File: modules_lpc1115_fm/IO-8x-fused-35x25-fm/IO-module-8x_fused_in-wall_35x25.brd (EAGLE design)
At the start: 35 x 25 mm, 75 parts, among them IC1 LPC1115, IC2 ATAES132A-SHEQ-T, Q2 ASFL, U1 EEPROM, X3 MICROMATCH-10

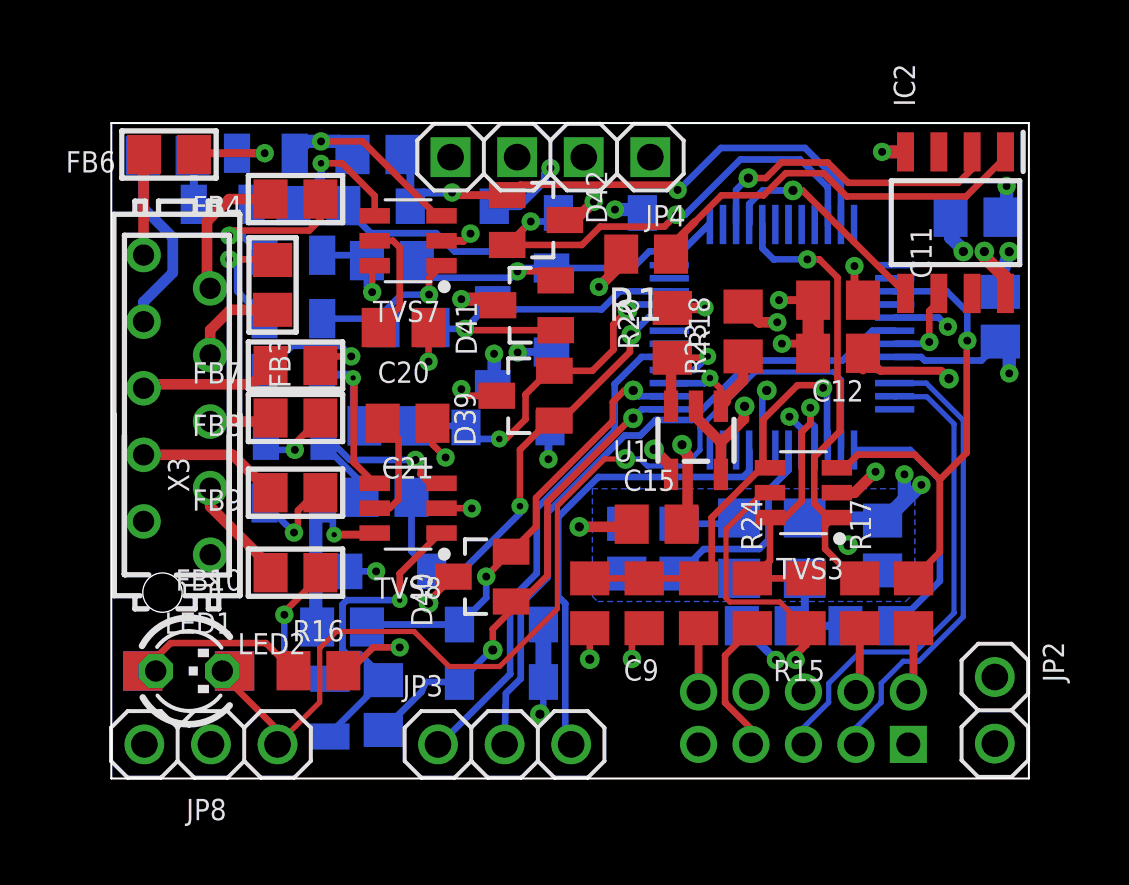
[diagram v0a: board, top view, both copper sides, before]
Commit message: [IOmodule8xUP]  moved power supply pins and SWD connector
consequences of changes in breakout board
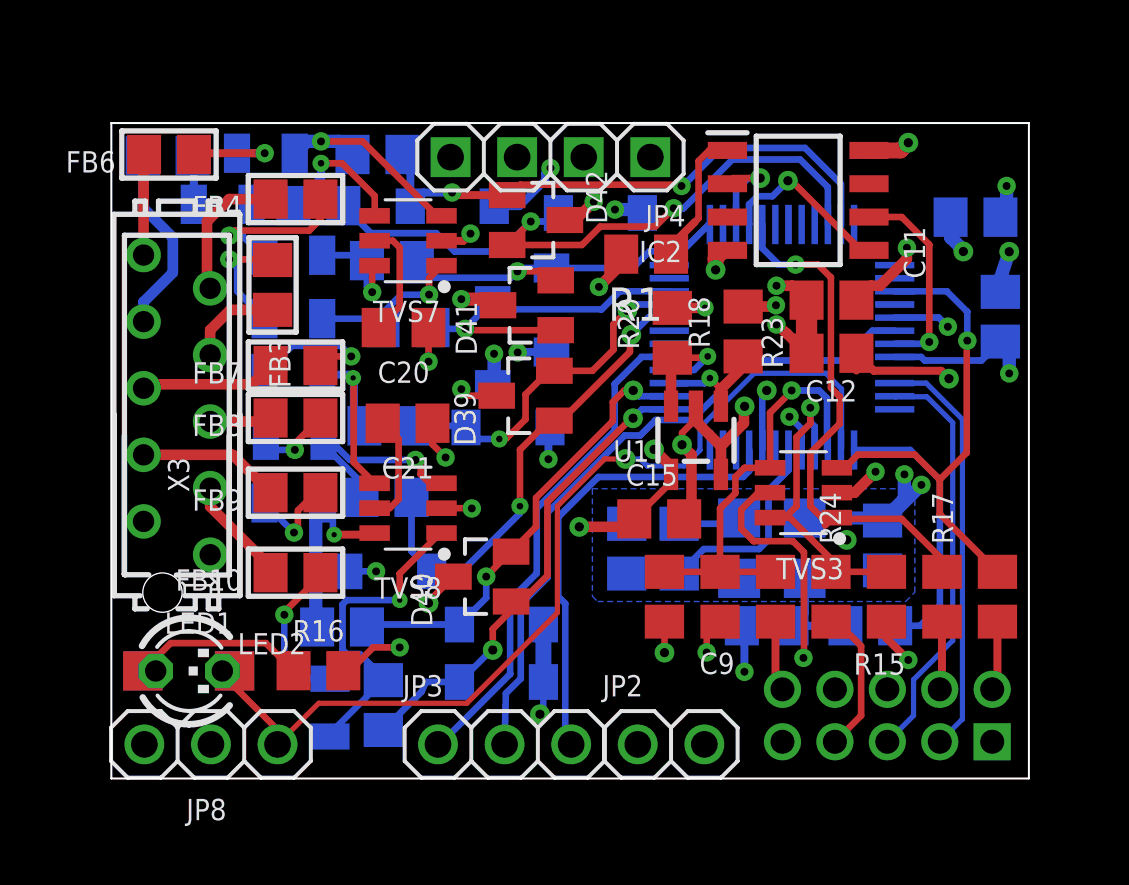
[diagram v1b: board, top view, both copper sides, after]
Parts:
- moved JP2 12.4 mm to (21.4, 1.30), turned to 0 degrees
- moved IC2 6.06 mm to (26.2, 22.1), turned to 0 degrees
- moved R19 3.21 mm to (33.8, 6.93)
- moved JP7 3.20 mm to (29.6, 2.40)
- moved R17 3.14 mm to (31.7, 6.93)
- moved R15 3.08 mm to (29.6, 6.93)
- moved R24 3.01 mm to (27.4, 6.93)
- moved R23 2.94 mm to (25.3, 6.93)
- moved C9 2.90 mm to (23.2, 6.93)
- moved R14 2.86 mm to (21.1, 6.93)
- moved C11 0.25 mm to (27.5, 18.2)
- moved C12 0.25 mm to (27.5, 16.2)
- moved C15 0.22 mm to (20.9, 9.90)
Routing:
- net N$19: track 15.4 -> 5.25 mm
- net MISO0: track 11.9 -> 3.75 mm
- net SCK1: track 3.35 -> 7.80 mm
- net GND: track 46.8 -> 50.6 mm
- net +3V3: track 53.3 -> 56.4 mm, vias 21 -> 22
- net SWCLK: track 17.6 -> 20.5 mm
- net ISP_TXD: track 18.5 -> 15.8 mm
- net PROG: track 39.9 -> 37.5 mm
- net ISP_RXD: track 17.6 -> 15.8 mm
- net MOSI0: track 8.59 -> 6.82 mm
- net ISP_EN: track 11.5 -> 13.1 mm
- net XTAL_EN: track 10.0 -> 10.6 mm

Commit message: [IOmodule8xUP]  added holes / change BB-fixing-pins from 4 to 2
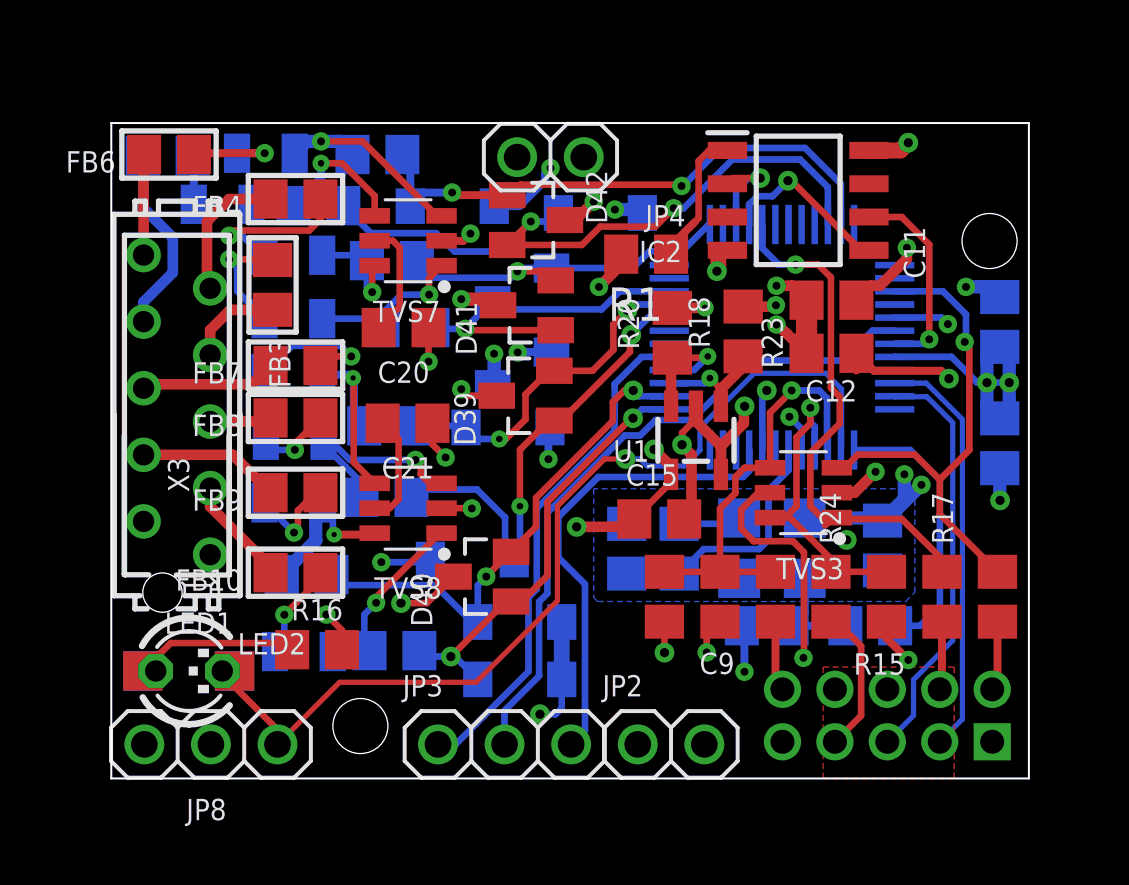
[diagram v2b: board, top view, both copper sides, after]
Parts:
- JP4: device pinhead_dmx:1X04 -> pinhead_dmx:1X02
- moved C13 4.83 mm to (33.9, 12.8), turned to 90 degrees
- moved C1 4.10 mm to (33.9, 17.4), turned to 270 degrees
- moved D35 3.18 mm to (13.8, 8.35)
- moved R45 2.41 mm to (7.45, 7.78)
- moved F21 2.36 mm to (7.34, 4.84), turned to 180 degrees
- moved R44 2.12 mm to (10.8, 4.88), turned to 180 degrees
- moved R16 0.80 mm to (7.85, 4.91)
- moved D37 0.71 mm to (15.6, 3.78)
- moved D38 0.71 mm to (15.6, 5.97)
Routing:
- net N$14: track 12.3 -> 7.26 mm
- net +3V3: track 56.4 -> 60.5 mm
- net IO2: track 16.9 -> 20.1 mm
- net N$7: track 5.89 -> 3.73 mm
- net IO1: track 18.4 -> 16.6 mm
- net N$20: track 7.89 -> 6.40 mm
- net GND: track 50.6 -> 51.9 mm
- added copper zone on layer 1, net NOGND

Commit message: [IOmodule8xUP] added JST ZH connector for I2C; reordered
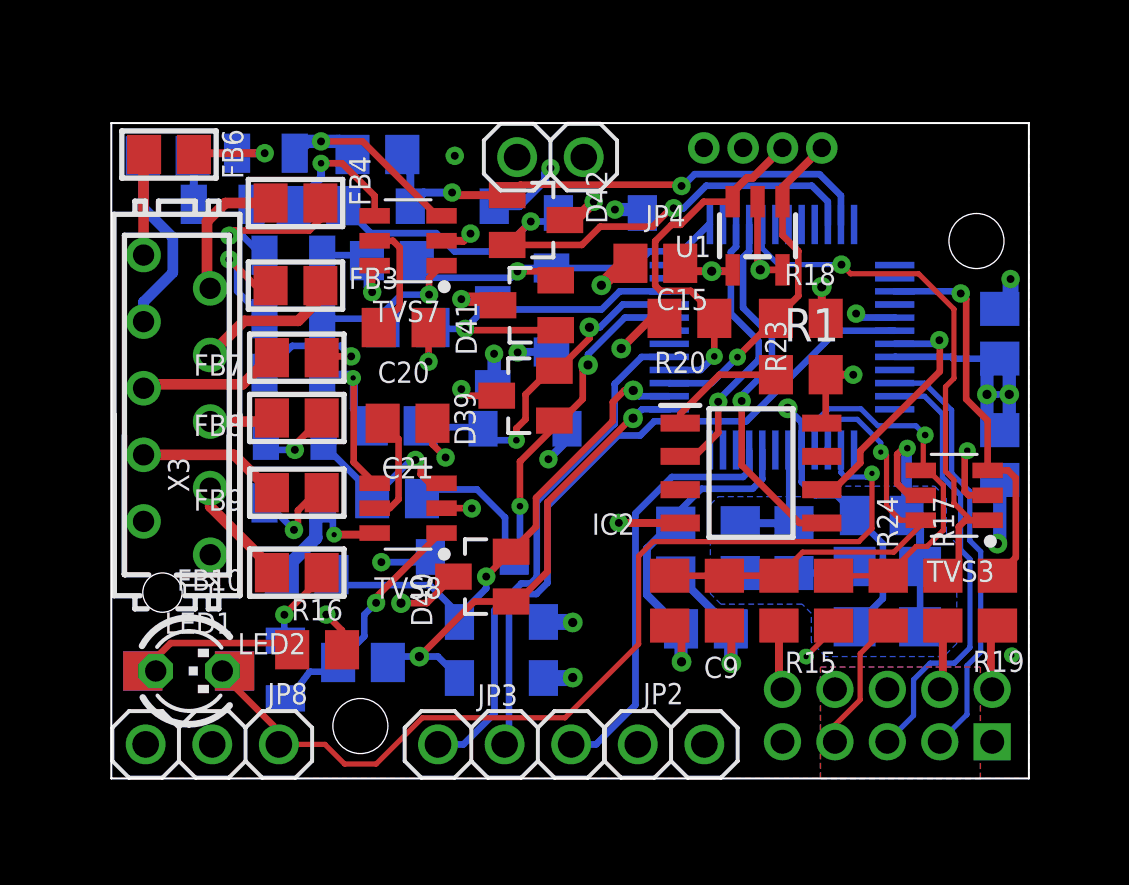
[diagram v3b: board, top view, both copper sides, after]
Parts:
- removed R26: 100k, rcl:R0805
- removed R27: 0R, rcl:R0805
- added JP1: B4B-ZR, jst:B4B-ZR
- moved C11 13.4 mm to (22.7, 5.71), flipped to the bottom, turned to 0 degrees
- moved IC2 10.6 mm to (24.4, 11.7)
- moved C15 9.75 mm to (20.8, 19.6), turned to 180 degrees
- moved C12 9.53 mm to (21.5, 8.77), flipped to the bottom, turned to 90 degrees
- moved U1 8.15 mm to (24.6, 20.7)
- moved R1 7.48 mm to (26.3, 15.4), turned to 0 degrees
- moved TVS3 5.75 mm to (32.1, 10.8)
- moved Q2 4.77 mm to (29.6, 6.94)
- moved C8 4.38 mm to (26.0, 8.79), turned to 270 degrees
- moved C7 4.33 mm to (24.0, 8.79), turned to 90 degrees
- moved R18 2.26 mm to (26.3, 17.6), turned to 0 degrees
- moved R24 2.19 mm to (29.6, 6.78)
- moved R15 2.02 mm to (27.5, 6.78)
- moved R44 1.28 mm to (9.60, 4.42)
- moved C14 1.15 mm to (29.4, 10.0), turned to 180 degrees
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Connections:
- removed net N$11: Q2.1, R26.1, R27.2
- net +3V3: now also JP1.2, Q2.1, X3.2; no longer R26.2, X3.1
- net GND: now also JP1.1, X3.1; no longer X3.2
- net ISP_EN: now also TVS3.4; no longer TVS3.6
- net RESET: now also TVS3.6; no longer TVS3.4
- net SCL: now also JP1.4
- net SDA: now also JP1.3
- net XTAL_EN: no longer R27.1
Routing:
- net XTAL_EN: track 10.6 -> 0.00 mm
- net SDA: track 4.93 -> 14.5 mm
- net SCL: track 5.13 -> 12.8 mm
- net +3V3: track 60.5 -> 52.9 mm, vias 22 -> 14
- net MOSI0: track 6.82 -> 14.2 mm
- net MISO0: track 3.75 -> 10.9 mm
- net XTALIN: track 9.68 -> 4.93 mm
- net SWDIO: track 19.0 -> 14.9 mm
- net N$11: track 4.07 -> 0.00 mm
- net GND: track 51.9 -> 54.5 mm
- net ISP_EN: track 13.1 -> 15.4 mm
- net N$14: track 7.26 -> 9.26 mm
- net IN5: track 3.65 -> 5.59 mm
- net IO1: track 16.6 -> 18.6 mm
- net EIB_IN: track 18.1 -> 16.2 mm
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- added copper zone on layer 1, net GND
- added copper zone on layer 16, net NOGND

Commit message: [IOmodule8xUP] massive re-arrangement
divided part so that 4 IOs are on TOP and 4 IOs on BOT
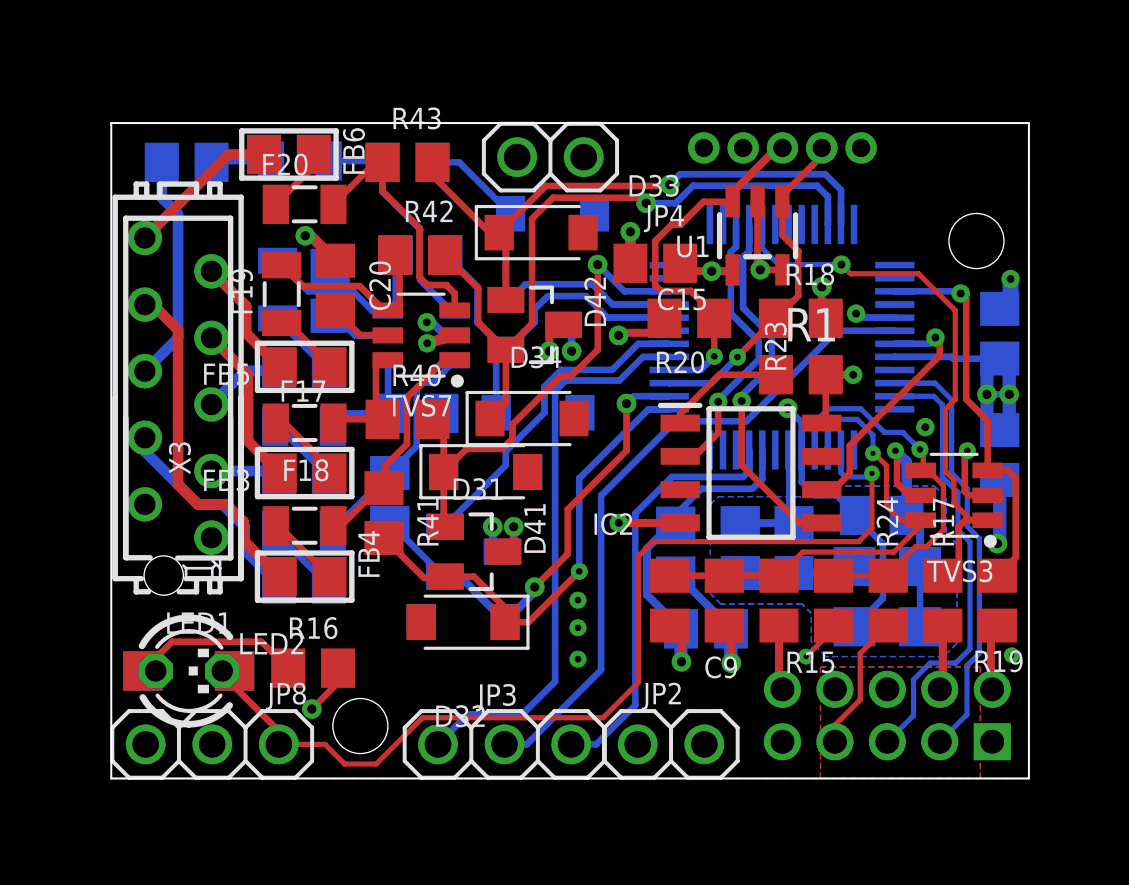
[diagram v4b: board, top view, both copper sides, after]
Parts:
- JP1: value B4B-ZR -> B5B-ZR; device jst:B4B-ZR -> jst:B5B-ZR
- moved FB4 14.3 mm to (7.38, 7.70)
- moved D32 12.4 mm to (13.4, 5.96), flipped to the top, turned to 180 degrees
- moved F18 10.3 mm to (7.38, 9.64), flipped to the top, turned to 0 degrees
- moved R47 10.1 mm to (11.3, 23.5)
- moved R44 9.72 mm to (11.7, 13.9)
- moved R41 9.63 mm to (10.4, 10.1), flipped to the top, turned to 270 degrees
- moved D41 9.61 mm to (13.8, 8.65), turned to 270 degrees
- moved FB5 9.60 mm to (7.38, 15.7), flipped to the top, turned to 180 degrees
- moved R46 9.34 mm to (11.8, 20.0)
- moved F21 9.31 mm to (7.35, 13.4), turned to 180 degrees
- moved FB7 8.55 mm to (2.88, 23.5), flipped to the bottom, turned to 0 degrees
- moved D36 8.27 mm to (16.8, 21.5)
- moved D34 8.26 mm to (16.0, 13.7), flipped to the top, turned to 0 degrees
- moved F24 8.10 mm to (7.20, 23.6)
- moved D37 7.87 mm to (14.3, 11.7)
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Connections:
- removed net IO114: IC1.10
- removed net N$14: F21.2, R44.1, TVS8.1
- removed net N$20: F22.2, R45.1, TVS8.6
- new net N$11: F18.2, R41.1, TVS7.1
- new net N$12: F17.2, R40.1, TVS7.6
- net IN6: now also X3.9; no longer X3.8
- net IN7: now also X3.8; no longer X3.9
- net IO1: now also D40.2, IC1.18; no longer D40.1, IC1.13
- net IO2: now also D40.1; no longer D40.2
- net IO6: now also IC1.13; no longer IC1.25
- net N$13: now also TVS8.6; no longer TVS8.3
- net N$16: now also F24.2, R47.1, TVS8.1; no longer F18.2, R41.1, TVS7.6
- net N$18: now also F21.2, R44.1, TVS8.4; no longer F17.2, R40.1, TVS7.1
- net N$9: now also F22.2, R45.1, TVS8.3; no longer F24.2, R47.1, TVS8.4
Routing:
- net GND: track 54.5 -> 40.8 mm, vias 23 -> 17
- net N$14: track 9.26 -> 0.00 mm, vias 1 -> 0
- net N$11: track 0.00 -> 8.77 mm
- net IN7: track 5.32 -> 13.3 mm
- net N$20: track 6.40 -> 0.00 mm, vias 1 -> 0
- net IO5: track 13.4 -> 18.8 mm
- net N$16: track 4.12 -> 8.97 mm, vias 1 -> 0
- net N$12: track 0.00 -> 4.60 mm
- net IO6: track 13.9 -> 18.0 mm
- net IO3: track 18.3 -> 14.9 mm, vias 2 -> 0
- net IN4: track 5.38 -> 8.75 mm
- net N$3: track 6.01 -> 2.85 mm, vias 1 -> 0
- net IN2: track 5.49 -> 8.26 mm
- net N$5: track 5.05 -> 2.29 mm, vias 1 -> 0
- net IN6: track 7.26 -> 4.73 mm
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
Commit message: [IOmodule8xUP]  optimized names & values positions; changed JP1 to 2mm
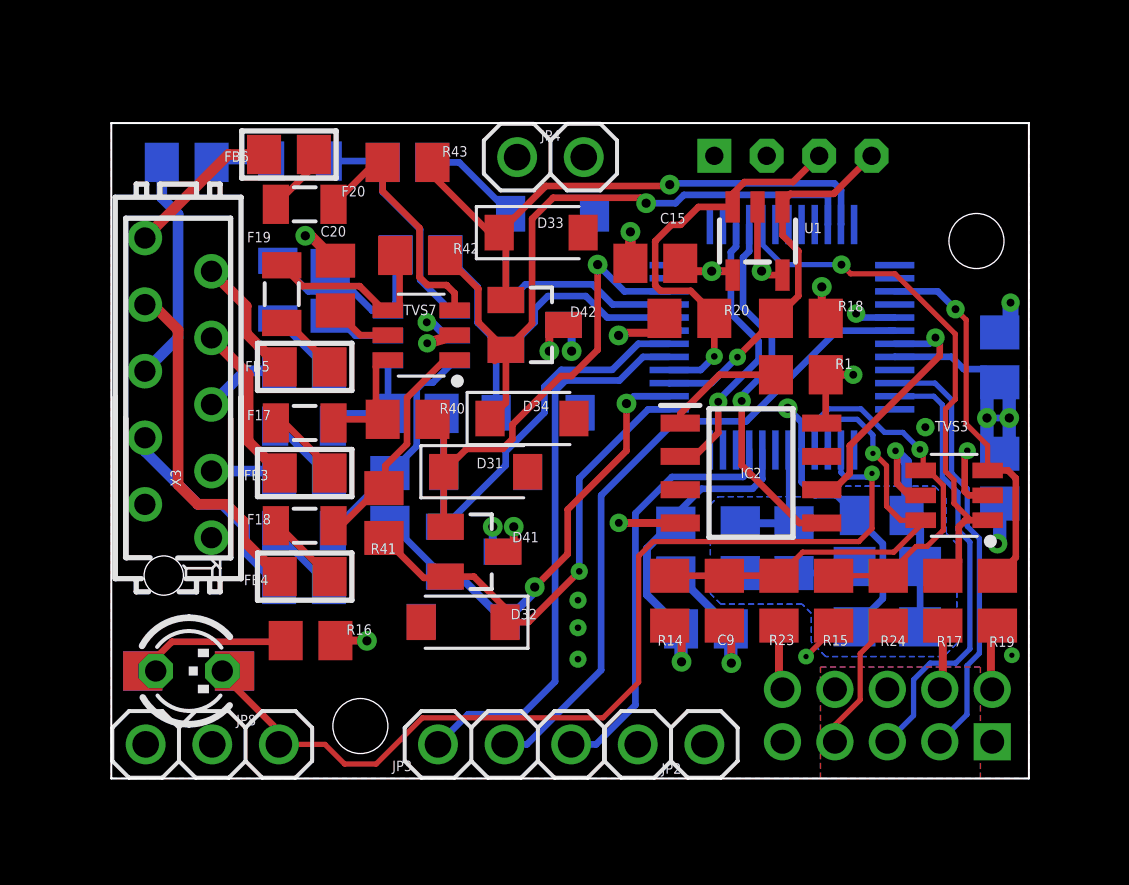
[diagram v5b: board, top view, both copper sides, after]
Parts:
- C1: value 1µ -> 100n
- C13: value 100n -> 1µ
- D31, D32, D33, D34, D35, D36, D37, D38: value DDZ9684 (3V3) -> DIODE
- JP1: value B5B-ZR -> B4B-PH-K-S; device jst:B5B-ZR -> con-JST PH:B4B-PH-K-S
- moved JP1 4.40 mm to (26.0, 23.8)
- moved R16 1.05 mm to (7.60, 5.26)
- moved C13 0.90 mm to (33.9, 11.4)
- moved C1 0.90 mm to (33.9, 16.1)
- moved U1 0.20 mm to (24.6, 20.5)
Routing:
- net SCL: track 12.8 -> 14.3 mm
- net SDA: track 14.5 -> 15.8 mm
- net GND: track 40.8 -> 39.8 mm
- net SWCLK: track 22.1 -> 21.5 mm
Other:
- board text added: "+"
- board text added: "+3V3"
- board text added: "-"
- board text added: "BUS-V"
- board text added: "EIB IN"
- board text added: "EIB OUT"
- board text added: "GND"
- board text added: "N.A."
- board text added: "SCL"
- board text added: "SDA"

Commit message: [IOmodule8xUP] optimized holes and markers; added vias;
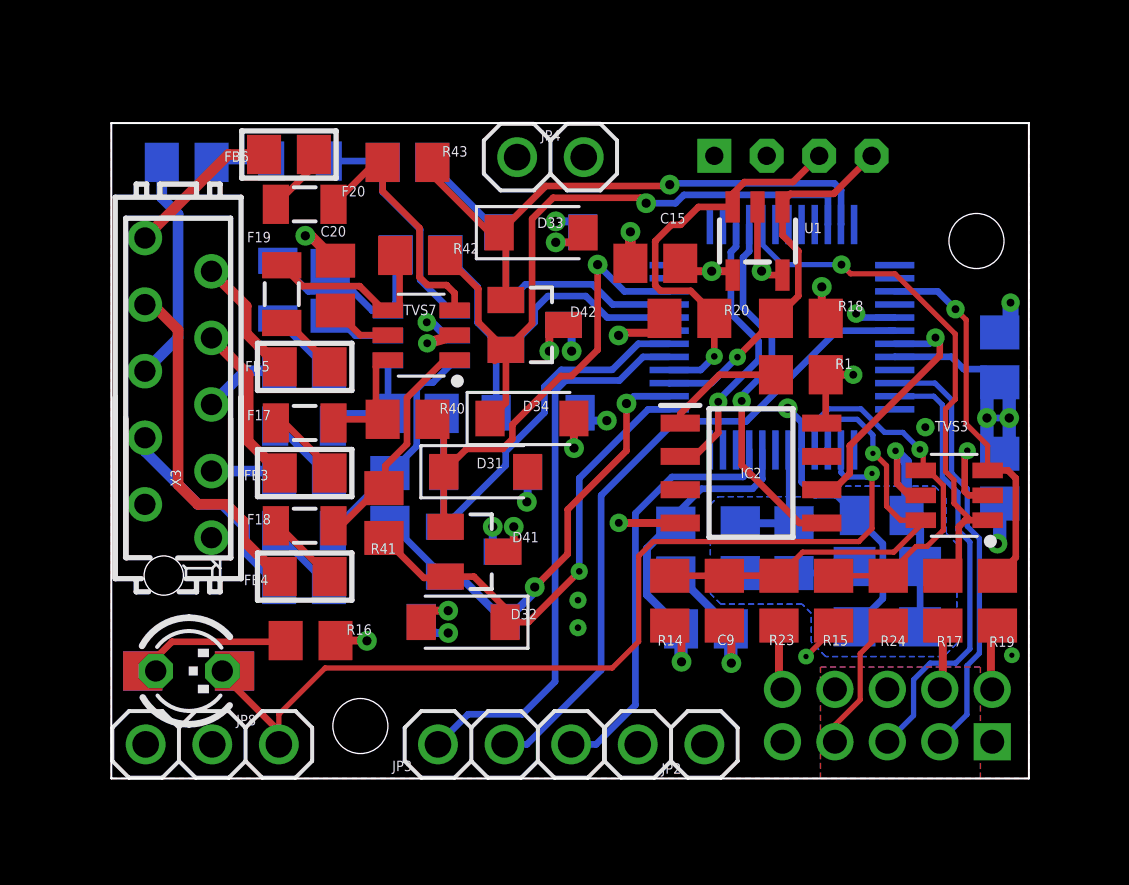
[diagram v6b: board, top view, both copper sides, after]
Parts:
- moved D36 0.83 mm to (16.4, 20.8)
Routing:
- net GND: track 39.8 -> 43.0 mm, vias 17 -> 23
- net PROG: track 38.2 -> 37.3 mm
- net IO4: track 14.0 -> 13.2 mm
